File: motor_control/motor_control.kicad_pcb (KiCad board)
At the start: 2 copper layers, 65 x 56 mm, 5 parts, among them J1 GPIO

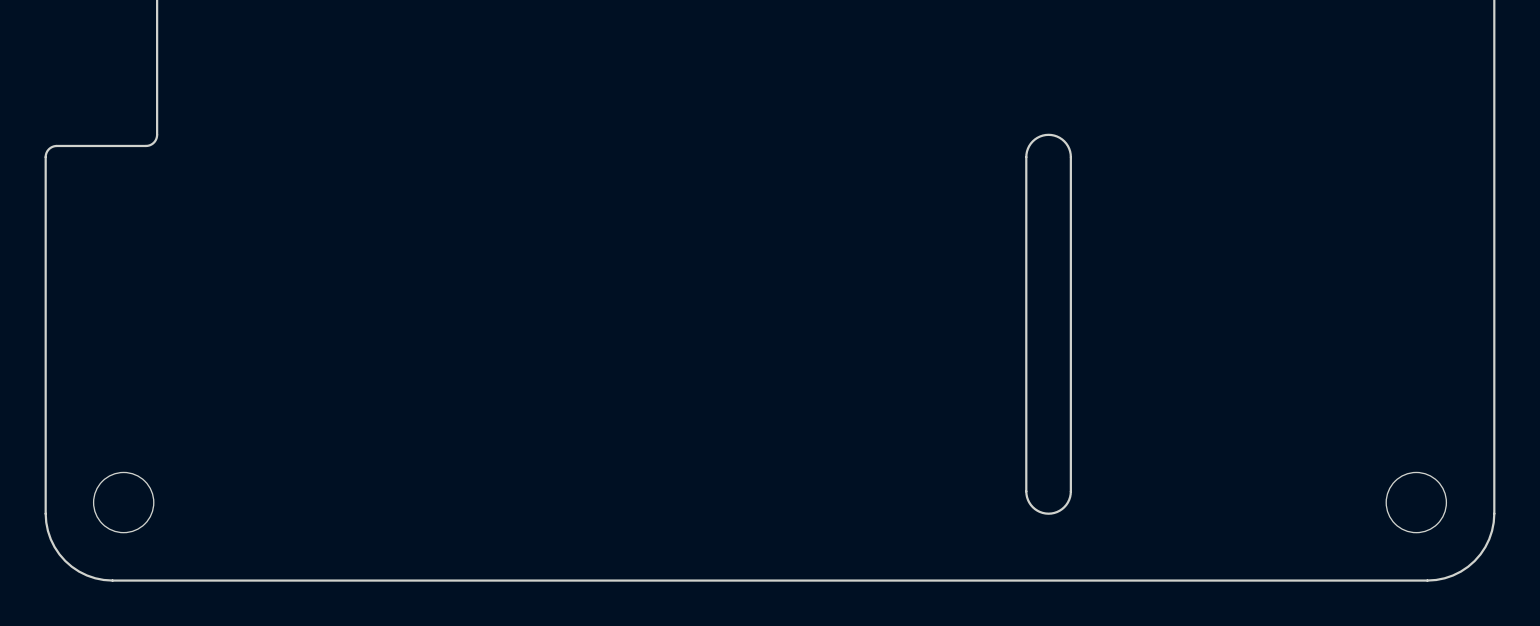
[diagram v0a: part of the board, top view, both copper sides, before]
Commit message: update board setup and edge cuts
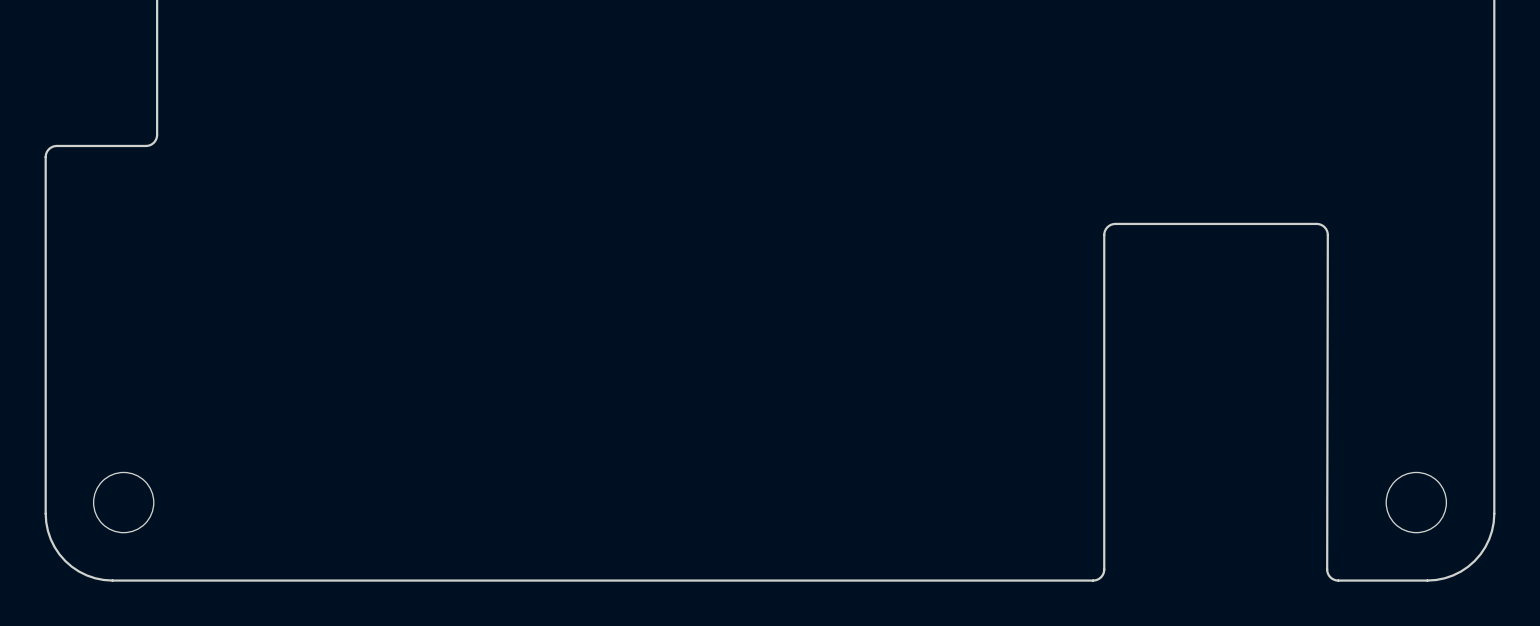
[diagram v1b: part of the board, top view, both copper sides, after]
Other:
- outline, holes or cut-outs redrawn
- copper layers 2 -> 4
- board text removed: "CAMERA (OPTIONAL)"
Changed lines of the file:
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@@
 	(layers
 		(0 "F.Cu" signal)
+		(4 "In1.Cu" signal)
+		(6 "In2.Cu" signal)
 		(2 "B.Cu" signal)
 		(9 "F.Adhes" user "F.Adhesive")
@@
 			(layer "F.Mask"
 				(type "Top Solder Mask")
-				(color "Green")
 				(thickness 0.01)
 			)
@@
 			)
 			(layer "dielectric 1"
-				(type "core")
-				(thickness 1.51)
+				(type "prepreg")
+				(thickness 0.1)
 				(material "FR4")
 				(epsilon_r 4.5)
 				(loss_tangent 0.02)
 			)
+			(layer "In1.Cu"
+				(type "copper")
+				(thickness 0.035)
+			)
+			(layer "dielectric 2"
+				(type "core")
+				(thickness 1.24)
+				(material "FR4")
+				(epsilon_r 4.5)
+				(loss_tangent 0.02)
+			)
+			(layer "In2.Cu"
+				(type "copper")
+				(thickness 0.035)
+			)
+			(layer "dielectric 3"
+				(type "prepreg")
+				(thickness 0.1)
+				(material "FR4")
+				(epsilon_r 4.5)
+				(loss_tangent 0.02)
+			)
 			(layer "B.Cu"
 				(type "copper")
@@
 			(layer "B.Mask"
 				(type "Bottom Solder Mask")
-				(color "Green")
 				(thickness 0.01)
 			)
@@
 				(type "Bottom Silk Screen")
 			)
-			(copper_finish "None")
+			(copper_finish "HAL lead-free")
 			(dielectric_constraints no)
 		)
@@
 			(psa4output no)
 			(plot_black_and_white yes)
-			(plotinvisibletext no)
 			(sketchpadsonfab no)
 			(plotpadnumbers no)
@@
 			(layer "F.CrtYd")
 		)
-		(fp_text user "${REFERENCE}"
-			(at 0.3 0 0)
-			(layer "F.Fab")
-			(hide yes)
-			(effects
-				(font
-					(size 1 1)
-					(thickness 0.15)
-				)
-			)
-		)
 		(pad "" np_thru_hole circle
 			(at 0 0)
 			(size 2.7 2.7)
 			(drill 2.7)
-			(layers "*.Cu" "*.Mask" "In1.Cu" "In2.Cu" "In3.Cu" "In4.Cu" "In5.Cu" "In6.Cu"
-				"In7.Cu" "In8.Cu" "In9.Cu" "In10.Cu" "In11.Cu" "In12.Cu" "In13.Cu" "In14.Cu"
-				"In15.Cu" "In16.Cu" "In17.Cu" "In18.Cu" "In19.Cu" "In20.Cu" "In21.Cu"
-				"In22.Cu" "In23.Cu" "In24.Cu" "In25.Cu" "In26.Cu" "In27.Cu" "In28.Cu"
-				"In29.Cu" "In30.Cu"
-			)
+			(layers "*.Cu" "*.Mask")
 		)
 		(embedded_fonts no)
@@
 			(layer "F.CrtYd")
 		)
-		(fp_text user "${REFERENCE}"
-			(at 0.3 0 0)
-			(layer "F.Fab")
-			(hide yes)
-			(effects
-				(font
-					(size 1 1)
-					(thickness 0.15)
-				)
-			)
-		)
 		(pad "" np_thru_hole circle
 			(at 0 0)
 			(size 2.7 2.7)
 			(drill 2.7)
-			(layers "*.Cu" "*.Mask" "In1.Cu" "In2.Cu" "In3.Cu" "In4.Cu" "In5.Cu" "In6.Cu"
-				"In7.Cu" "In8.Cu" "In9.Cu" "In10.Cu" "In11.Cu" "In12.Cu" "In13.Cu" "In14.Cu"
-				"In15.Cu" "In16.Cu" "In17.Cu" "In18.Cu" "In19.Cu" "In20.Cu" "In21.Cu"
-				"In22.Cu" "In23.Cu" "In24.Cu" "In25.Cu" "In26.Cu" "In27.Cu" "In28.Cu"
-				"In29.Cu" "In30.Cu"
-			)
+			(layers "*.Cu" "*.Mask")
 		)
 		(embedded_fonts no)
@@
 			(layer "F.CrtYd")
 		)
-		(fp_text user "${REFERENCE}"
-			(at 0.3 0 0)
-			(layer "F.Fab")
-			(hide yes)
-			(effects
-				(font
-					(size 1 1)
-					(thickness 0.15)
-				)
-			)
-		)
 		(pad "" np_thru_hole circle
 			(at 0 0)
 			(size 2.7 2.7)
 			(drill 2.7)
-			(layers "*.Cu" "*.Mask" "In1.Cu" "In2.Cu" "In3.Cu" "In4.Cu" "In5.Cu" "In6.Cu"
-				"In7.Cu" "In8.Cu" "In9.Cu" "In10.Cu" "In11.Cu" "In12.Cu" "In13.Cu" "In14.Cu"
-				"In15.Cu" "In16.Cu" "In17.Cu" "In18.Cu" "In19.Cu" "In20.Cu" "In21.Cu"
-				"In22.Cu" "In23.Cu" "In24.Cu" "In25.Cu" "In26.Cu" "In27.Cu" "In28.Cu"
-				"In29.Cu" "In30.Cu"
-			)
+			(layers "*.Cu" "*.Mask")
 		)
 		(embedded_fonts no)
@@
 			(layer "F.CrtYd")
 		)
-		(fp_text user "${REFERENCE}"
-			(at 0.3 0 0)
-			(layer "F.Fab")
-			(hide yes)
-			(effects
-				(font
-					(size 1 1)
-					(thickness 0.15)
-				)
-			)
-		)
 		(pad "" np_thru_hole circle
 			(at 0 0)
 			(size 2.7 2.7)
 			(drill 2.7)
-			(layers "*.Cu" "*.Mask" "In1.Cu" "In2.Cu" "In3.Cu" "In4.Cu" "In5.Cu" "In6.Cu"
-				"In7.Cu" "In8.Cu" "In9.Cu" "In10.Cu" "In11.Cu" "In12.Cu" "In13.Cu" "In14.Cu"
-				"In15.Cu" "In16.Cu" "In17.Cu" "In18.Cu" "In19.Cu" "In20.Cu" "In21.Cu"
-				"In22.Cu" "In23.Cu" "In24.Cu" "In25.Cu" "In26.Cu" "In27.Cu" "In28.Cu"
-				"In29.Cu" "In30.Cu"
-			)
+			(layers "*.Cu" "*.Mask")
 		)
 		(embedded_fonts no)
@@
 		(layer "Dwgs.User")
 	)
+	(gr_line
+		(start 146.998 100)
+		(end 103 100)
+		(stroke
+			(width 0.1)
+			(type solid)
+		)
+		(layer "Edge.Cuts")
+	)
+	(gr_arc
+		(start 147.498 84.498)
+		(mid 147.644447 84.144447)
+		(end 147.998 83.998)
+		(stroke
+			(width 0.1)
+			(type default)
+		)
+		(layer "Edge.Cuts")
+	)
 	(gr_arc
 		(start 100.5 63.5)
@@
 	)
 	(gr_line
+		(start 147.498 84.498)
+		(end 147.498 99.5)
+		(stroke
+			(width 0.1)
+			(type solid)
+		)
+		(layer "Edge.Cuts")
+	)
+	(gr_line
 		(start 165 97)
 		(end 165 47)
@@
 		(layer "Edge.Cuts")
 	)
-	(gr_line
-		(start 146 81)
-		(end 146 96)
-		(stroke
-			(width 0.1)
-			(type solid)
-		)
-		(layer "Edge.Cuts")
-	)
-	(gr_line
-		(start 144 96)
-		(end 144 81)
-		(stroke
-			(width 0.1)
-			(type solid)
+	(gr_arc
+		(start 158.00097 100)
+		(mid 157.647074 99.853211)
+		(end 157.500971 99.499031)
+		(stroke
+			(width 0.1)
+			(type default)
 		)
 		(layer "Edge.Cuts")
@@
 		(layer "Edge.Cuts")
 	)
+	(gr_arc
+		(start 157.03003 83.998)
+		(mid 157.383926 84.144789)
+		(end 157.53003 84.498969)
+		(stroke
+			(width 0.1)
+			(type default)
+		)
+		(layer "Edge.Cuts")
+	)
 	(gr_line
-		(start 103 100)
+		(start 158.00097 100)
 		(end 162 100)
 		(stroke
@@
 	)
 	(gr_arc
-		(start 144 81)
-		(mid 145 80)
-		(end 146 81)
-		(stroke
-			(width 0.1)
-			(type solid)
+		(start 147.498 99.5)
+		(mid 147.351553 99.853553)
+		(end 146.998 100)
+		(stroke
+			(width 0.1)
+			(type default)
 		)
 		(layer "Edge.Cuts")
@@
 	)
 	(gr_line
+		(start 157.03003 83.998)
+		(end 147.998 83.998)
+		(stroke
+			(width 0.1)
+			(type solid)
+		)
+		(layer "Edge.Cuts")
+	)
+	(gr_line
 		(start 105 64)
 		(end 105 80)
@@
 		(layer "Edge.Cuts")
 	)
-	(gr_arc
-		(start 146 96)
-		(mid 145 97)
-		(end 144 96)
-		(stroke
-			(width 0.1)
-			(type solid)
-		)
-		(layer "Edge.Cuts")
-	)
 	(gr_line
 		(start 100 81)
@@
 		(mid 104.853553 63.646447)
 		(end 105 64)
+		(stroke
+			(width 0.1)
+			(type solid)
+		)
+		(layer "Edge.Cuts")
+	)
+	(gr_line
+		(start 157.500971 99.499031)
+		(end 157.53003 84.498969)
 		(stroke
 			(width 0.1)
@@
 	(gr_text "DISPLAY (OPTIONAL)"
 		(at 102.5 72 90)
-		(layer "Dwgs.User")
-		(effects
-			(font
-				(size 1 1)
-				(thickness 0.15)
-			)
-		)
-	)
-	(gr_text "CAMERA (OPTIONAL)"
-		(at 145 88.5 90)
 		(layer "Dwgs.User")
 		(effects
@@
 		)
 	)
-	(group ""
-		(members "1811fd1a-b55e-4d16-931d-f9ec6a9e16f7" "79c07597-5ab9-4d26-b4b3-a70ae9dcd11d"
-			"81e492f6-268f-4ce2-bb45-32834e67e85b" "b6c3db4f-e418-4da3-aef6-5010435bcf13"
-			"d4c39290-1388-499e-abdc-d2c7dce5190a"
-		)
-	)

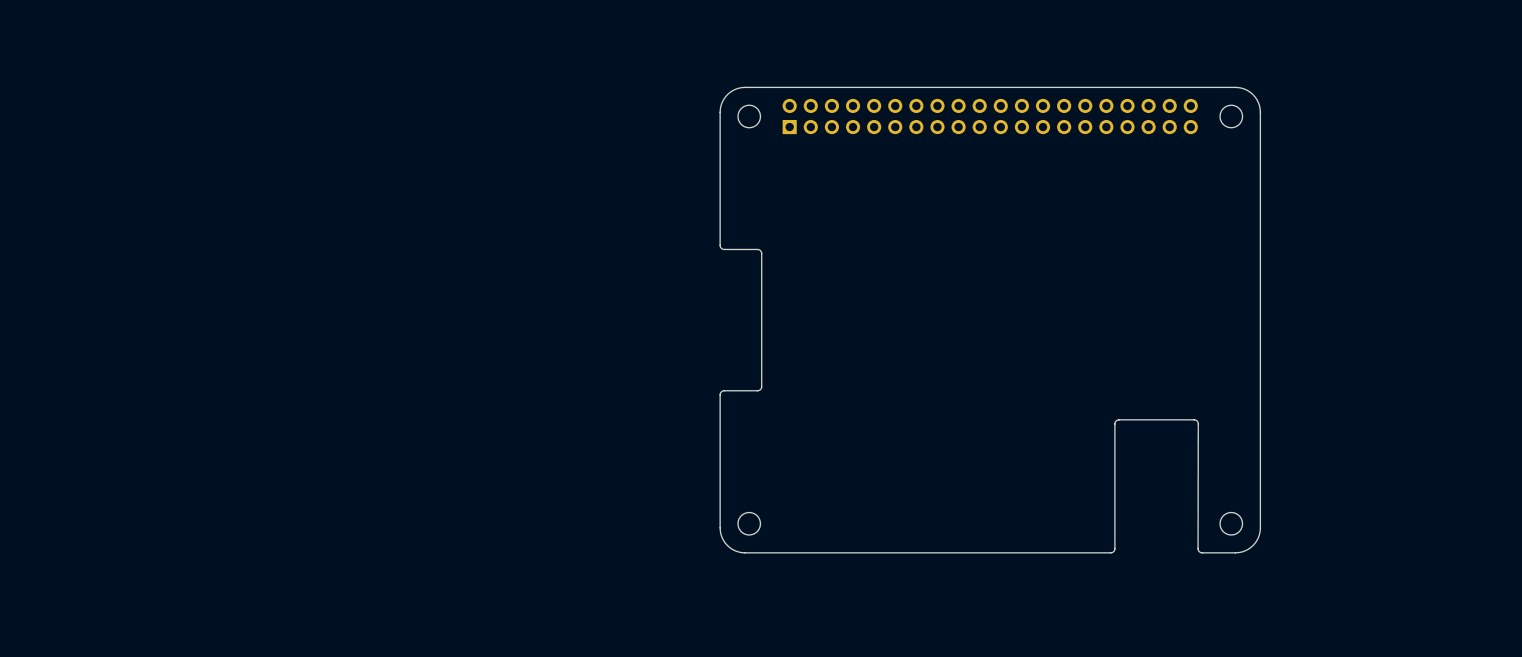
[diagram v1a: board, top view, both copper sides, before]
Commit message: update pico footprint
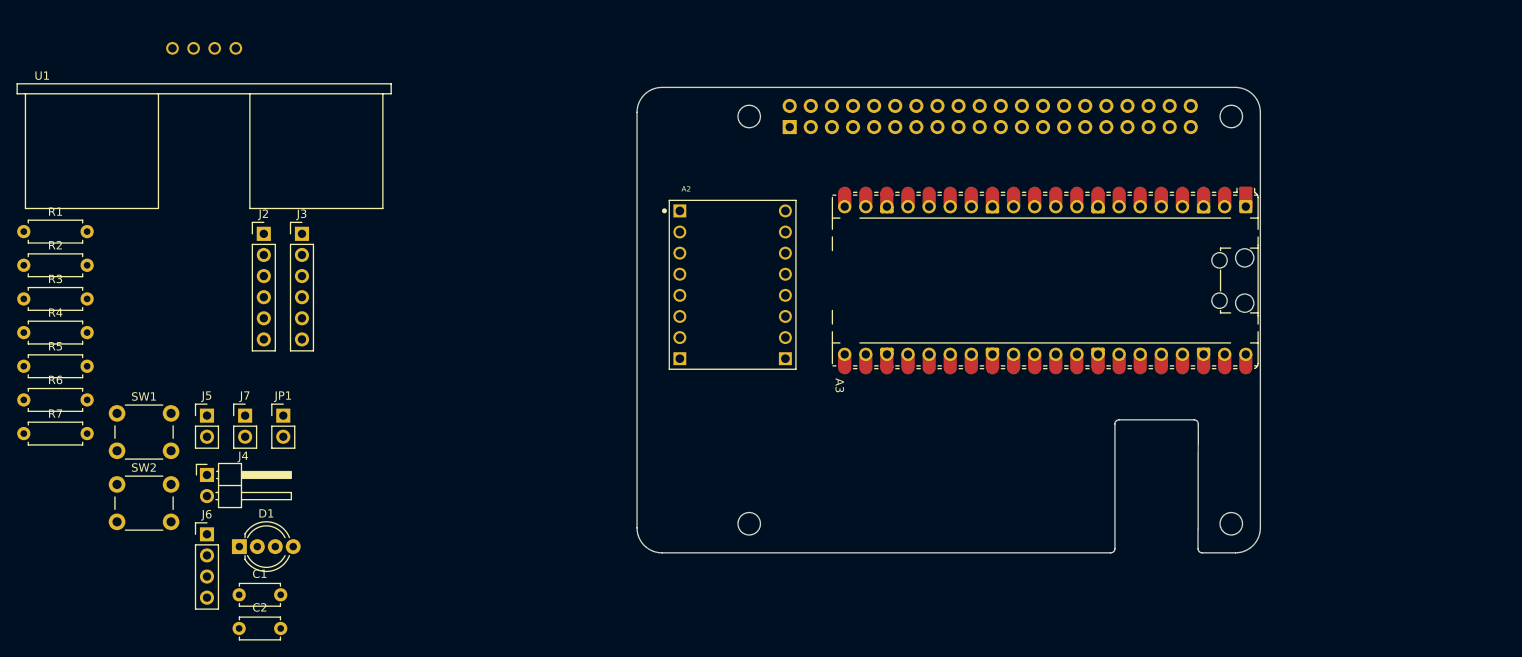
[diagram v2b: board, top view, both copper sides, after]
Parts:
- added A2: Pololu_Breakout_TB6612FNG, POLOLU-713:SHIELD_POLOLU-713, F.Cu at (101.5, 67.8)
- added A3: RaspberryPi_Pico, Module:RaspberryPi_Pico_Common_Unspecified, F.Cu at (139.1, 67.2)
- added C1: 100n, Capacitor_THT:C_Disc_D4.7mm_W2.5mm_P5.00mm, F.Cu at (42.1, 105.0)
- added C2: 100n, Capacitor_THT:C_Disc_D4.7mm_W2.5mm_P5.00mm, F.Cu at (42.1, 109.1)
- added D1: LED_RKGB, LED_THT:LED_D5.0mm-4_RGB_Wide_Pins, F.Cu at (42.2, 99.2)
- added J2: Conn_Motor_01x06, Connector_PinHeader_2.54mm:PinHeader_1x06_P2.54mm_Vertical, F.Cu at (45.1, 61.6)
- added J3: Conn_Motor_01x06, Connector_PinHeader_2.54mm:PinHeader_1x06_P2.54mm_Vertical, F.Cu at (49.7, 61.6)
- added J4: Conn_MOT_POW_01x02, Connector_PinHeader_2.54mm:PinHeader_1x02_P2.54mm_Horizontal, F.Cu at (38.3, 90.6)
- added J5: Conn_UART_01x02, Connector_PinHeader_2.54mm:PinHeader_1x02_P2.54mm_Vertical, F.Cu at (38.3, 83.5)
- added J6: Conn_SPI_01x04, Connector_PinHeader_2.54mm:PinHeader_1x04_P2.54mm_Vertical, F.Cu at (38.3, 97.8)
- added J7: Conn_I2C_01x02, Connector_PinHeader_2.54mm:PinHeader_1x02_P2.54mm_Vertical, F.Cu at (42.9, 83.5)
- added JP1: Jumper_2_Open, Connector_PinHeader_2.54mm:PinHeader_1x02_P2.54mm_Vertical, F.Cu at (47.4, 83.5)
- added R1: 220R, Resistor_THT:R_Axial_DIN0207_L6.3mm_D2.5mm_P7.62mm_Horizontal, F.Cu at (16.2, 61.4)
- added R2: 220R, Resistor_THT:R_Axial_DIN0207_L6.3mm_D2.5mm_P7.62mm_Horizontal, F.Cu at (16.2, 65.4)
- added R3: 220R, Resistor_THT:R_Axial_DIN0207_L6.3mm_D2.5mm_P7.62mm_Horizontal, F.Cu at (16.2, 69.5)
- added R4: 1K, Resistor_THT:R_Axial_DIN0207_L6.3mm_D2.5mm_P7.62mm_Horizontal, F.Cu at (16.2, 73.5)
- added R5: 1K, Resistor_THT:R_Axial_DIN0207_L6.3mm_D2.5mm_P7.62mm_Horizontal, F.Cu at (16.2, 77.5)
- added R6: 1.2K, Resistor_THT:R_Axial_DIN0207_L6.3mm_D2.5mm_P7.62mm_Horizontal, F.Cu at (16.2, 81.6)
- added R7: 2K, Resistor_THT:R_Axial_DIN0207_L6.3mm_D2.5mm_P7.62mm_Horizontal, F.Cu at (16.2, 85.7)
- added SW1: PU, Button_Switch_THT:SW_PUSH_6mm, F.Cu at (27.4, 83.2)
- added SW2: PD, Button_Switch_THT:SW_PUSH_6mm, F.Cu at (27.4, 91.8)
- added U1: HC-SR04, HC-SR04:XCVR_HC-SR04, F.Cu at (37.9, 39.3)
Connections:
- net +3V3 renamed +3.3V
- J1 pad 3: /GPIO2/SDA1 -> /SDA1
- J1 pad 5: /GPIO3/SCL1 -> /SCL1
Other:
- board size 65 x 56 mm -> 75 x 56 mm
- board text removed: "DISPLAY (OPTIONAL)"

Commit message: layout v1
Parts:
- added J8: VBUS_OUT, Connector_PinHeader_2.54mm:PinHeader_1x02_P2.54mm_Vertical, F.Cu at (163.1, 83.0)
- J2: value Conn_Motor_01x06 -> MotA
- J3: value Conn_Motor_01x06 -> MotB
- J4: value Conn_MOT_POW_01x02 -> MOT_POW
- J5: value Conn_UART_01x02 -> UART
- J6: value Conn_SPI_01x04 -> SPI
- J7: value Conn_I2C_01x02 -> I2C
- JP1: value Jumper_2_Open -> 5V_VBUS
- moved R3 130.2 mm to (145.7, 82.6), turned to -90 degrees
- moved J5 127.8 mm to (163.0, 55.8), turned to -90 degrees
- moved R2 127.5 mm to (142.5, 82.6), turned to -90 degrees
- moved R1 125.0 mm to (139.4, 82.6), turned to -90 degrees
- moved J6 124.5 mm to (155.4, 55.8), turned to -90 degrees
- moved R7 116.3 mm to (127.7, 52.7)
- moved R6 114.4 mm to (127.7, 56.0)
- moved R5 111.8 mm to (127.7, 85.9)
- moved R4 109.8 mm to (125.3, 85.9), turned to 180 degrees
- moved SW2 108.0 mm to (135.3, 97.3), turned to 180 degrees
- moved J7 103.7 mm to (142.8, 55.8), turned to -90 degrees
- moved D1 103.7 mm to (145.7, 94.9), turned to 180 degrees
- moved C2 96.9 mm to (135.3, 82.6), turned to 180 degrees
- moved SW1 91.7 mm to (118.6, 92.8)
- moved C1 83.9 mm to (122.9, 82.6)
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
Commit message: wiring v1
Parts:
- moved JP1 21.3 mm to (116.0, 53.9)
- moved J2 12.7 mm to (97.3, 55.4), turned to 90 degrees
- moved J3 12.7 mm to (97.3, 83.3), turned to 90 degrees
- moved C1 8.39 mm to (130.0, 87.1), turned to 90 degrees
- moved R4 4.45 mm to (125.1, 90.3)
- moved R5 4.44 mm to (127.7, 90.3)
- moved R7 3.63 mm to (129.2, 56.0)
- moved R6 3.54 mm to (129.2, 52.8)
- moved U1 3.29 mm to (93.3, 72.0)
- moved SW1 0.84 mm to (118.6, 93.6)
- moved SW2 0.84 mm to (135.3, 98.1)
- moved C2 0.52 mm to (135.1, 82.1), turned to -90 degrees
- moved J7 0.10 mm to (142.7, 55.8)
- moved J8 0.09 mm to (163.0, 83.0), turned to 0 degrees
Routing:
- net VBUS: track 0.00 -> 110.7 mm, vias 0 -> 1
- net +3V3: track 0.00 -> 97.9 mm, vias 0 -> 1
- net Net-(U1-ECHO): track 0.00 -> 56.9 mm, vias 0 -> 1
- net VSYS: track 0.00 -> 56.7 mm
- net /TRIG: track 0.00 -> 48.6 mm
- net /SDA1: track 0.00 -> 39.4 mm
- net /SCL1: track 0.00 -> 35.5 mm
- net /C2A: track 0.00 -> 31.9 mm
- net /C2B: track 0.00 -> 29.2 mm
- net /C1A: track 0.00 -> 27.0 mm
- net /C1B: track 0.00 -> 24.8 mm
- net VMOT: track 0.00 -> 18.8 mm
- net /BO2: track 0.00 -> 18.6 mm
- net /AO2: track 0.00 -> 18.5 mm
- net /STBY: track 0.00 -> 18.1 mm
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- added copper zone on B.Cu, net GND
- added copper zone on F.Cu, net GND
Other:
- board text added: "+3v3"
- board text added: "5V"
- board text added: "A1"
- board text added: "A2"
- board text added: "AO1"
- board text added: "AO2"
- board text added: "B1"
- board text added: "B2"
- board text added: "BO1"
- board text added: "BO2"
- board text added: "C1A"
- board text added: "C1B"
- board text added: "C2A"
- board text added: "C2B"
- board text added: "Csn0"
- board text added: "GND"
- board text added: "GP0"
- board text added: "GP15"
- board text added: "GP16"
- board text added: "SCK0"
- board text added: "SCL"
- board text added: "SDA"
- board text added: "SRX0"
- board text added: "STX0"
- board text added: "URX0"
- board text added: "UTX0"
- board text added: "VBUS"
- board text added: "VMOT"
